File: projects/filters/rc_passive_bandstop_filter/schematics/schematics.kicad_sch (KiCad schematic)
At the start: 3 parts, among them J1 15V, U1 LM741

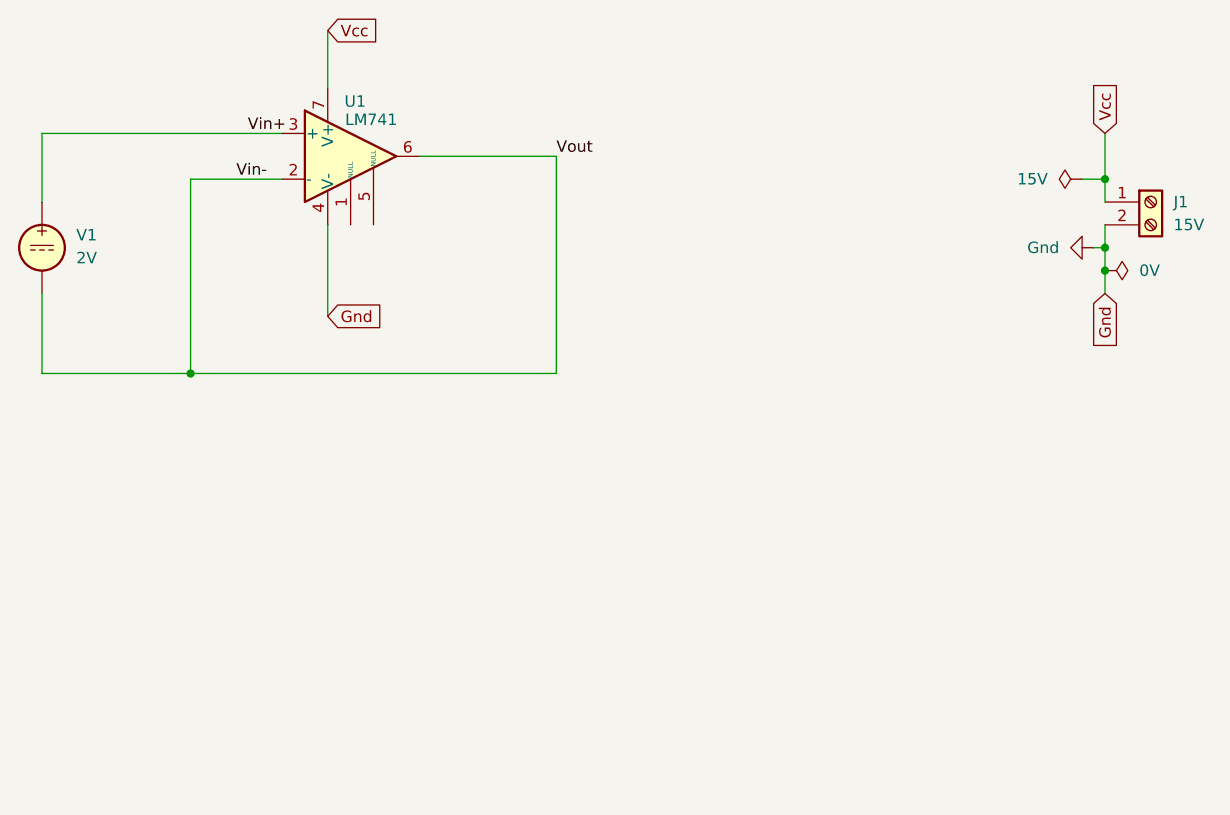
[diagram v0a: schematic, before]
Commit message: feat: add RC Passive Bandstop filter and unity gain projects
Adds a new project on RC Passive Bandstop filter including schematics,
simulations, and explanations.

Adds a unity gain amplifier project with updated schematics and
documentation.

Breaking changes: None

Resolves: None
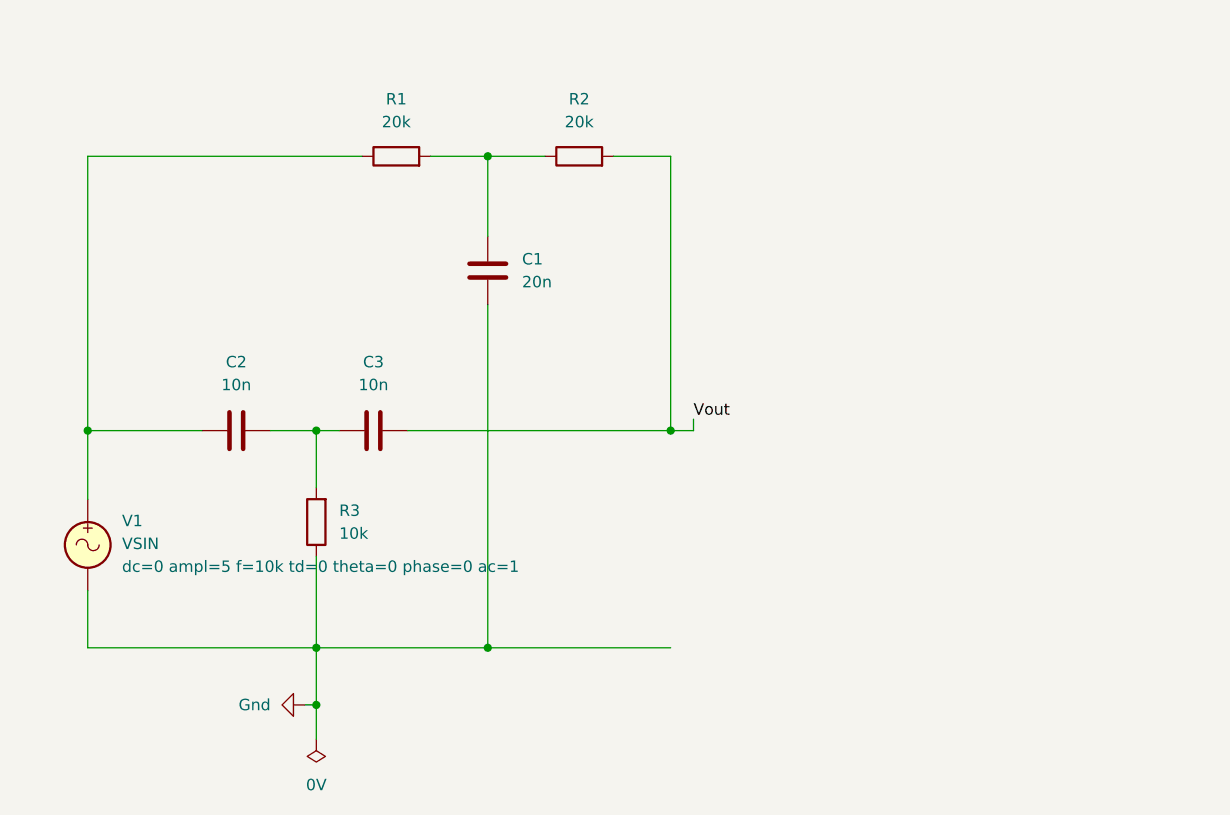
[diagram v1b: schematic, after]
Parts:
- removed J1: 15V, TerminalBlock:TerminalBlock_Xinya_XY308-2.54-2P_1x02_P2.54mm_Horizontal, symbol Connector:Screw_Terminal_01x02
- removed U1: LM741, symbol Amplifier_Operational:LM741
- removed V1: 2V, symbol Simulation_SPICE:VDC
- added C1: 20n, symbol Device:C
- added C2, C3: 10n, symbol Device:C
- added R1, R2: 20k, symbol Device:R
- added R3: 10k, symbol Device:R
- added V1: VSIN, symbol Simulation_SPICE:VSIN
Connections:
- net Gnd: now also C1.2, R3.1, V1.2
- new net: C2.1, R1.1, V1.1
- new net: C1.1, R1.2, R2.1
- new net: C2.2, C3.1, R3.2
- new net Vout: C3.2, R2.2
